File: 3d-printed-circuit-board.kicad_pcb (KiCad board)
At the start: 2 copper layers, 40.5 x 40.5 mm, 8 parts

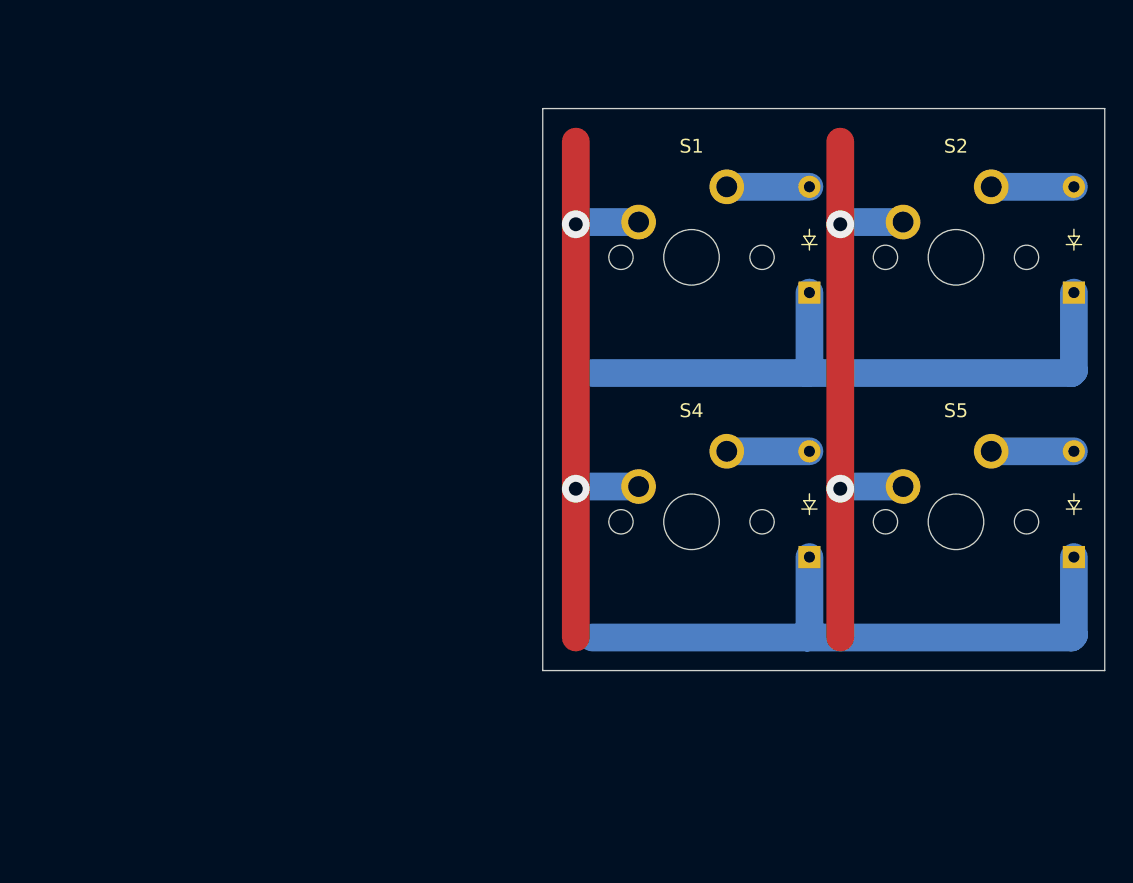
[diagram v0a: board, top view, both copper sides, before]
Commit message: Add column stagger
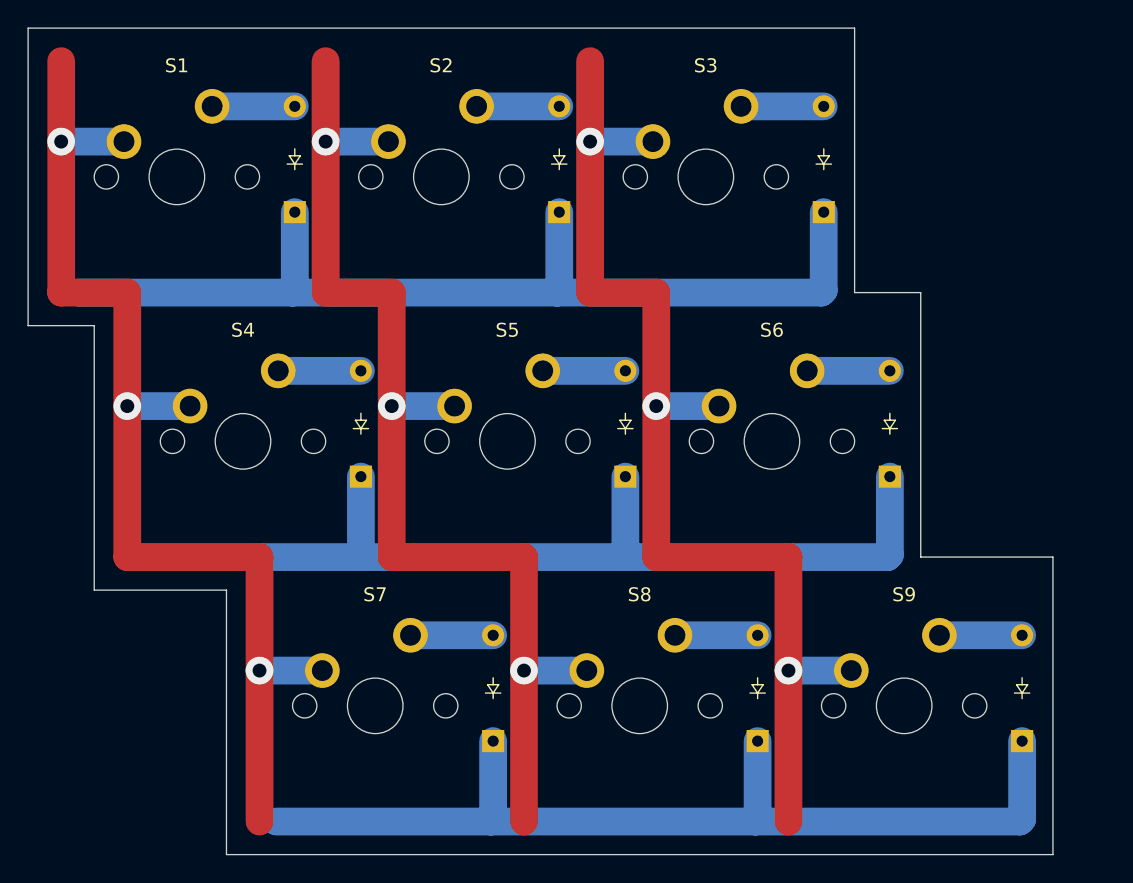
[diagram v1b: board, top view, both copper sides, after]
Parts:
- added D3: Diode, ScottoKeebs_Components:Diode_DO-35, F.Cu at (159.9, 92.9)
- added D6: Diode, ScottoKeebs_Components:Diode_DO-35, F.Cu at (164.7, 112.0)
- added D7: Diode, ScottoKeebs_Components:Diode_DO-35, F.Cu at (136.1, 131.0)
- added D8: Diode, ScottoKeebs_Components:Diode_DO-35, F.Cu at (155.2, 131.0)
- added D9: Diode, ScottoKeebs_Components:Diode_DO-35, F.Cu at (174.2, 131.0)
- added S3: Keyswitch, ScottoKeebs_MX:MX_PCB_1.00u, F.Cu at (151.4, 90.4)
- added S6: Keyswitch, ScottoKeebs_MX:MX_PCB_1.00u, F.Cu at (156.2, 109.4)
- added S7: Keyswitch, ScottoKeebs_MX:MX_PCB_1.00u, F.Cu at (127.6, 128.5)
- added S8: Keyswitch, ScottoKeebs_MX:MX_PCB_1.00u, F.Cu at (146.7, 128.5)
- added S9: Keyswitch, ScottoKeebs_MX:MX_PCB_1.00u, F.Cu at (165.7, 128.5)
- moved D2 37.5 mm to (140.9, 92.9)
- moved S1 37.5 mm to (113.3, 90.4)
- moved D1 37.5 mm to (121.8, 92.9)
- moved S2 37.5 mm to (132.4, 90.4)
- moved D5 32.8 mm to (145.7, 112.0)
- moved S4 32.8 mm to (118.1, 109.4)
- moved D4 32.8 mm to (126.6, 112.0)
- moved S5 32.8 mm to (137.2, 109.4)
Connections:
- net Net-(D1-K) renamed ROW0
- net Net-(D4-K) renamed ROW1
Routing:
- net COL2: track 0.00 -> 82.6 mm, vias 0 -> 3
- net ROW2: track 0.00 -> 71.2 mm
- net COL1: track 45.1 -> 82.9 mm, vias 2 -> 3
- net COL0: track 45.1 -> 82.9 mm, vias 2 -> 3
- net ROW0: track 46.2 -> 71.2 mm
- net ROW1: track 46.2 -> 71.2 mm
- net Net-(D9-A): track 0.00 -> 5.95 mm
- net Net-(D8-A): track 0.00 -> 5.95 mm
- net Net-(D7-A): track 0.00 -> 5.95 mm
- net Net-(D6-A): track 0.00 -> 5.95 mm
- net Net-(D3-A): track 0.00 -> 5.95 mm
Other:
- board size 40.5 x 40.5 mm -> 73.8 x 59.5 mm
